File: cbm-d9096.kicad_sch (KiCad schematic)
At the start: 30 parts, among them J1 IEEE488 Header, J2 SD CARD, J3 WP/CD Jumper, J4 LED, J5 RESET, J6 Barrel_Jack, J7 Alt PWR, U1 ATmega1284-P, U2 75160, U3 75161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

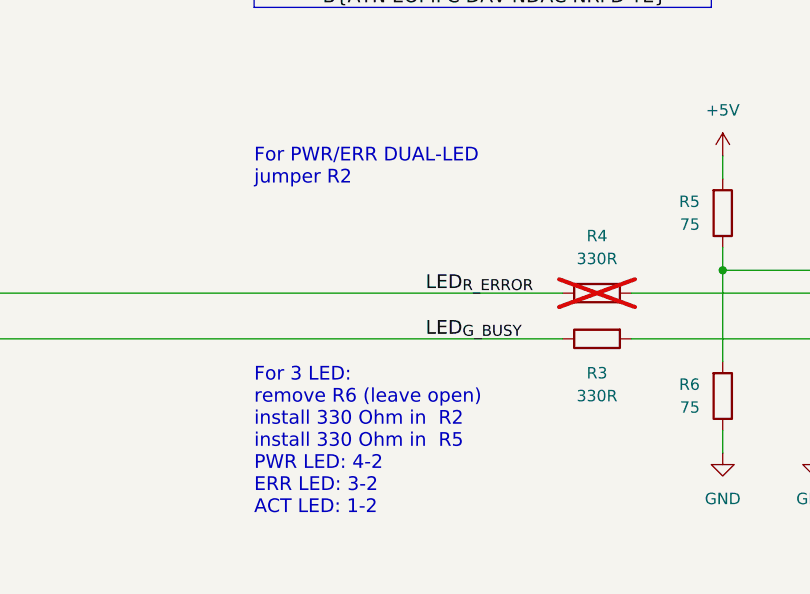
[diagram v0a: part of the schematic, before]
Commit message: - fixed schematics text referring to R4 as R2
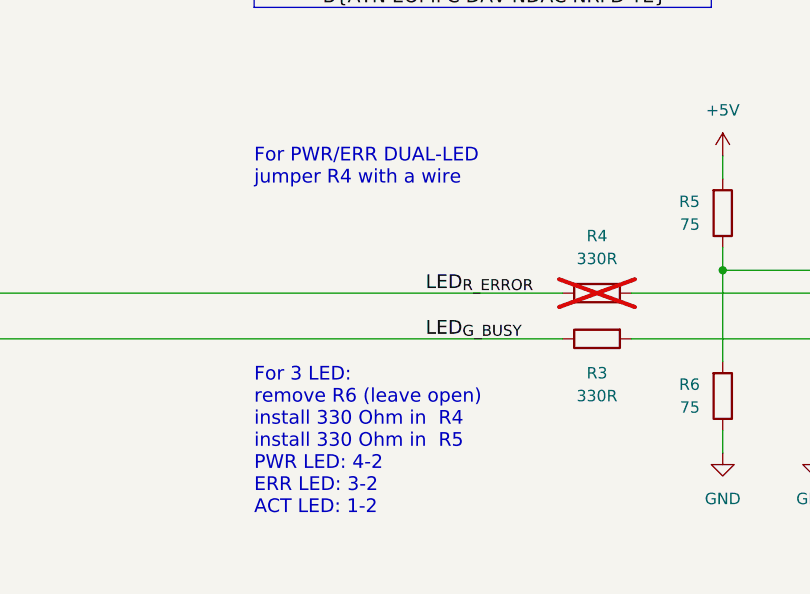
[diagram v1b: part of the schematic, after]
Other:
- note added: "For 3 LED: remove R6 (leave open) install 330 Ohm in R4 install 330 Ohm in R5 PWR LED: 4-2 ERR LED: 3-2 ACT LED: 1-2"
- note added: "For PWR/ERR DUAL-LED jumper R4 with a wire"
- note removed: "For 3 LED: remove R6 (leave open) install 330 Ohm in R2 install 330 Ohm in R5 PWR LED: 4-2 ERR LED: 3-2 ACT LED: 1-2"
- note removed: "For PWR/ERR DUAL-LED jumper R2"
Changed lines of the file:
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@@
 		)
 	)
-	(text "For 3 LED:\nremove R6 (leave open)\ninstall 330 Ohm in  R2\ninstall 330 Ohm in  R5\nPWR LED: 4-2\nERR LED: 3-2\nACT LED: 1-2"
+	(text "For 3 LED:\nremove R6 (leave open)\ninstall 330 Ohm in  R4\ninstall 330 Ohm in  R5\nPWR LED: 4-2\nERR LED: 3-2\nACT LED: 1-2"
 		(exclude_from_sim no)
 		(at 260.35 184.15 0)
@@
 		)
 	)
-	(text "For PWR/ERR DUAL-LED\njumper R2"
+	(text "For PWR/ERR DUAL-LED\njumper R4 with a wire"
 		(exclude_from_sim no)
 		(at 260.35 153.67 0)

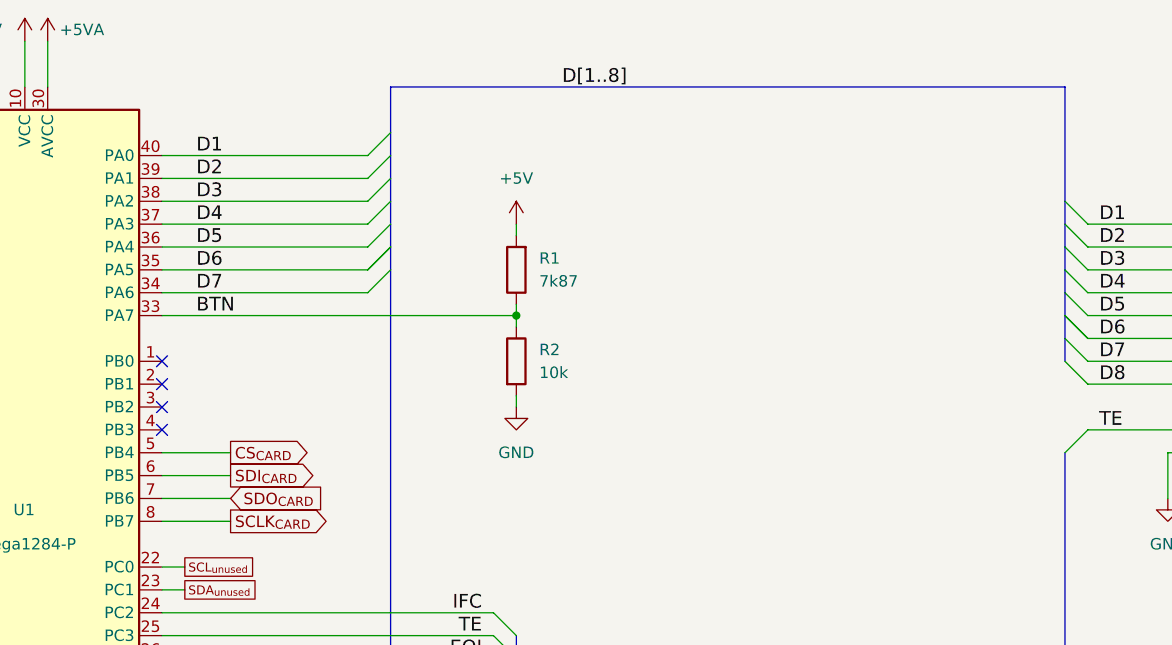
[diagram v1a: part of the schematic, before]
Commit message: Custom Firmware
Added custom firmware by Andry Gray omitting the button checks in firmware, allowing for the removal of the removal of the resistor divider formed by resistors R1 and R2
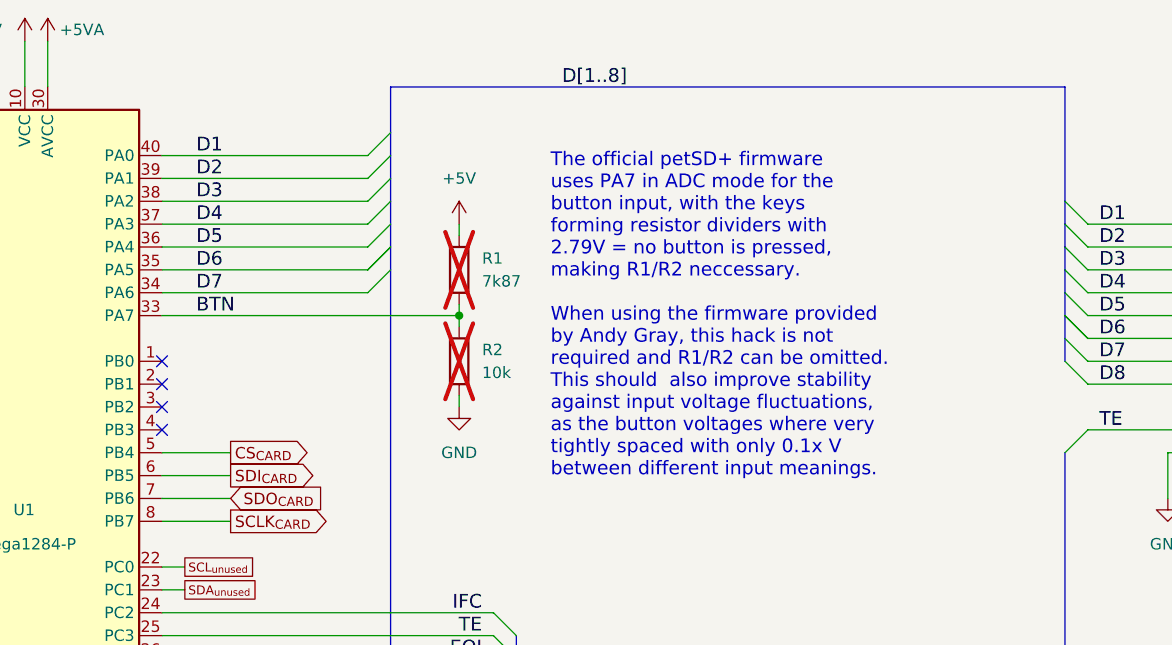
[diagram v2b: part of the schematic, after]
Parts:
- R1, R2: now not fitted
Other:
- note added: "The official petSD+ firmware uses PA7 in ADC mode for the button input, with the keys forming resistor dividers with 2.79V = no button is pressed, making R1/R2 neccessary. When using the firmware provided by Andy Gray, this hack is not required and R1/R2 can be omitted. This should also improve stability against input voltage fluctuations, as the button voltages where very tightly spaced with onl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"
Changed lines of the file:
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@@
 	)
 	(junction
-		(at 152.4 54.61)
+		(at 146.05 54.61)
 		(diameter 0)
 		(color 0 0 0 0)
@@
 	(wire
 		(pts
-			(xy 152.4 53.34) (xy 152.4 54.61)
+			(xy 146.05 53.34) (xy 146.05 54.61)
 		)
 		(stroke
@@
 	(wire
 		(pts
-			(xy 113.03 54.61) (xy 152.4 54.61)
+			(xy 113.03 54.61) (xy 146.05 54.61)
 		)
 		(stroke
@@
 	(wire
 		(pts
-			(xy 152.4 45.72) (xy 152.4 44.45)
+			(xy 146.05 45.72) (xy 146.05 44.45)
 		)
 		(stroke
@@
 	(wire
 		(pts
-			(xy 152.4 64.77) (xy 152.4 63.5)
+			(xy 146.05 64.77) (xy 146.05 63.5)
 		)
 		(stroke
@@
 	(wire
 		(pts
-			(xy 152.4 55.88) (xy 152.4 54.61)
+			(xy 146.05 55.88) (xy 146.05 54.61)
 		)
 		(stroke
@@
 		)
 	)
+	(text "The official petSD+ firmware\nuses PA7 in ADC mode for the\nbutton input, with the keys\nforming resistor dividers with\n2.79V = no button is pressed,\nmaking R1/R2 neccessary.\n\nWhen using the firmware provided\nby Andy Gray, this hack is not\nrequired and R1/R2 can be omitted.\nThis should  also improve stability\nagainst input voltage fluctuations,\nas the button voltages where very\ntightly spaced with only 0.1x V\nbetween different input meanings."
+		(exclude_from_sim no)
+		(at 156.21 54.61 0)
+		(effects
+			(font
+				(size 1.524 1.524)
+			)
+			(justify left)
+		)
+	)
 	(text "CBM D9096"
 		(exclude_from_sim no)
@@
 	(symbol
 		(lib_id "Device:R")
-		(at 152.4 49.53 180)
+		(at 146.05 49.53 180)
 		(unit 1)
 		(exclude_from_sim no)
 		(in_bom yes)
 		(on_board yes)
-		(dnp no)
+		(dnp yes)
 		(fields_autoplaced yes)
 		(property "Reference" "R1"
-			(at 154.94 48.2599 0)
+			(at 148.59 48.2599 0)
 			(effects
 				(font
@@
 		)
 		(property "Value" "7k87"
-			(at 154.94 50.7999 0)
+			(at 148.59 50.7999 0)
 			(effects
 				(font
@@
 		)
 		(property "Footprint" "cbm-d9096_lib_fp:R_Axial_DIN0207_L6.3mm_D2.5mm_P10.16mm_Horizontal"
-			(at 154.178 49.53 90)
+			(at 147.828 49.53 90)
 			(effects
 				(font
@@
 		)
 		(property "Datasheet" "~"
-			(at 152.4 49.53 0)
+			(at 146.05 49.53 0)
 			(effects
 				(font
@@
 		)
 		(property "Description" "Resistor"
-			(at 152.4 49.53 0)
+			(at 146.05 49.53 0)
 			(effects
 				(font
@@
 		(lib_name "GND_1")
 		(lib_id "power:GND")
-		(at 152.4 64.77 0)
+		(at 146.05 64.77 0)
 		(unit 1)
 		(exclude_from_sim no)
@@
 		(fields_autoplaced yes)
 		(property "Reference" "#PWR012"
-			(at 152.4 71.12 0)
+			(at 146.05 71.12 0)
 			(effects
 				(font
@@
 		)
 		(property "Value" "GND"
-			(at 152.4 69.85 0)
+			(at 146.05 69.85 0)
 			(effects
 				(font
@@
 		)
 		(property "Footprint" ""
-			(at 152.4 64.77 0)
+			(at 146.05 64.77 0)
 			(effects
 				(font
@@
 		)
 		(property "Datasheet" ""
-			(at 152.4 64.77 0)
+			(at 146.05 64.77 0)
 			(effects
 				(font
@@
 		)
 		(property "Description" "Power symbol creates a global label with name \"GND\" , ground"
-			(at 152.4 64.77 0)
+			(at 146.05 64.77 0)
 			(effects
 				(font
@@
 	(symbol
 		(lib_id "Device:R")
-		(at 152.4 59.69 0)
+		(at 146.05 59.69 0)
 		(unit 1)
 		(exclude_from_sim no)
 		(in_bom yes)
 		(on_board yes)
-		(dnp no)
+		(dnp yes)
 		(fields_autoplaced yes)
 		(property "Reference" "R2"
-			(at 154.94 58.4199 0)
+			(at 148.59 58.4199 0)
 			(effects
 				(font
@@
 		)
 		(property "Value" "10k"
-			(at 154.94 60.9599 0)
+			(at 148.59 60.9599 0)
 			(effects
 				(font
@@
 		)
 		(property "Footprint" "cbm-d9096_lib_fp:R_Axial_DIN0207_L6.3mm_D2.5mm_P10.16mm_Horizontal"
-			(at 150.622 59.69 90)
+			(at 144.272 59.69 90)
 			(effects
 				(font
@@
 		)
 		(property "Datasheet" "~"
-			(at 152.4 59.69 0)
+			(at 146.05 59.69 0)
 			(effects
 				(font
@@
 		)
 		(property "Description" "Resistor"
-			(at 152.4 59.69 0)
+			(at 146.05 59.69 0)
 			(effects
 				(font
@@
 		(lib_name "+5V_1")
 		(lib_id "power:+5V")
-		(at 152.4 44.45 0)
+		(at 146.05 44.45 0)
 		(mirror y)
 		(unit 1)
@@
 		(fields_autoplaced yes)
 		(property "Reference" "#PWR020"
-			(at 152.4 48.26 0)
+			(at 146.05 48.26 0)
 			(effects
 				(font
@@
 		)
 		(property "Value" "+5V"
-			(at 152.4 39.37 0)
+			(at 146.05 39.37 0)
 			(effects
 				(font
@@
 		)
 		(property "Footprint" ""
-			(at 152.4 44.45 0)
+			(at 146.05 44.45 0)
 			(effects
 				(font
@@
 		)
 		(property "Datasheet" ""
-			(at 152.4 44.45 0)
+			(at 146.05 44.45 0)
 			(effects
 				(font
@@
 		)
 		(property "Description" "Power symbol creates a global label with name \"+5V\""
-			(at 152.4 44.45 0)
+			(at 146.05 44.45 0)
 			(effects
 				(font

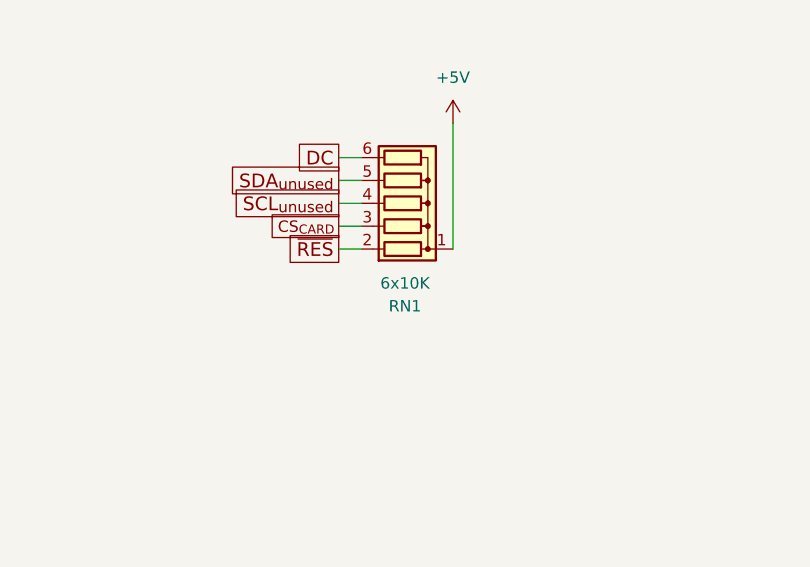
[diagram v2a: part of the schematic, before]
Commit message: RN1 Description fix
RN1 was described as 6x10K, changed to the correct 5*6K
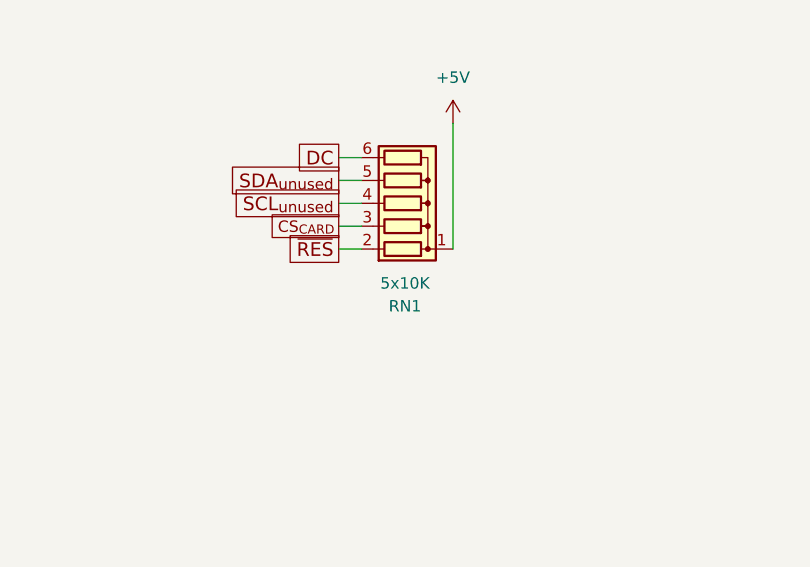
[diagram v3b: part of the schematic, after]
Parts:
- RN1: value 6x10K -> 5x10K
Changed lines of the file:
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@@
 			)
 		)
-		(property "Value" "6x10K"
+		(property "Value" "5x10K"
 			(at 243.586 226.06 90)
 			(effects
